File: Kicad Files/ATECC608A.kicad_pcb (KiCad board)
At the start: 2 copper layers, 26.7 x 22.8 mm, 17 parts, among them J1 Conn_01x04, U1 ATECC608A-SSHDA

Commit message: logos review
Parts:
- added G***: LOGO, Aesthetics:SDA, B.Cu at (168.6, 47.0)
- added G***: LOGO, Aesthetics:SCL, B.Cu at (166.2, 47.1)
- added G***: LOGO, Aesthetics:GND, B.Cu at (163.6, 47.1)
- added G***: LOGO, Aesthetics:3v3, B.Cu at (161.0, 47.1)
- J1: moved to B.Cu
- moved REF** 1.41 mm to (155.3, 43.0)
- moved G*** 0.15 mm to (164.8, 34.5)
- turned J1 to 270 degrees

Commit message: logos
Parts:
- moved G*** 0.48 mm to (166.0, 47.1)
- moved G*** 0.45 mm to (168.5, 47.1)
- moved G*** 0.40 mm to (163.4, 47.1)
- moved G*** 0.40 mm to (160.8, 47.1)
- moved G*** 0.14 mm to (163.7, 47.0)
- moved G*** 0.10 mm to (161.0, 47.0)
- moved G*** 0.08 mm to (166.2, 47.0)
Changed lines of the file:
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@@
-(kicad_pcb (version 20171130) (host pcbnew "(5.1.4-0-10_14)")
+(kicad_pcb (version 20171130) (host pcbnew "(5.1.4)-1")
   (general
     (thickness 1.6)
@@
     (35 F.Paste user)
     (36 B.SilkS user)
-    (37 F.SilkS user hide)
+    (37 F.SilkS user)
     (38 B.Mask user)
     (39 F.Mask user)
@@
     (43 Eco2.User user)
     (44 Edge.Cuts user)
-    (45 Margin user)
+    (45 Margin user hide)
     (46 B.CrtYd user)
     (47 F.CrtYd user)
@@
   )
   (module Aesthetics:SCL (layer B.Cu)
-    (at 166.15 47.125 270)
+    (at 166.15 47.05 270)
     (fp_text reference G*** (at 0 0 90) (layer B.SilkS) hide
       (effects (font (size 1.524 1.524) (thickness 0.3)) (justify mirror))
@@
   )
   (module Aesthetics:GND (layer B.Cu)
-    (at 163.575 47.1 270)
+    (at 163.703 47.05 270)
     (fp_text reference G*** (at 0 0 90) (layer B.SilkS) hide
       (effects (font (size 1.524 1.524) (thickness 0.3)) (justify mirror))
@@
   )
   (module Aesthetics:3v3 (layer B.Cu)
-    (at 161 47.15 270)
+    (at 161 47.05 270)
     (fp_text reference G*** (at 0 0 90) (layer B.SilkS) hide
       (effects (font (size 1.524 1.524) (thickness 0.3)) (justify mirror))
@@
   )
   (module GND (layer F.Cu)
-    (at 163.5 47.45 90)
+    (at 163.4238 47.0555 90)
     (fp_text reference G*** (at 0 0 90) (layer F.SilkS) hide
       (effects (font (size 1.524 1.524) (thickness 0.3)))
@@
   )
   (module 3v3 (layer F.Cu)
-    (at 160.9 47.45 90)
+    (at 160.8238 47.0555 90)
     (fp_text reference G*** (at 0 0 90) (layer F.SilkS) hide
       (effects (font (size 1.524 1.524) (thickness 0.3)))
@@
   )
   (module SCL (layer F.Cu)
-    (at 166.35 47.4 90)
+    (at 166.0144 47.0535 90)
     (fp_text reference G*** (at 0 0 90) (layer F.SilkS) hide
       (effects (font (size 1.524 1.524) (thickness 0.3)))
@@
   )
   (module SDA (layer F.Cu)
-    (at 168.6 47.5 90)
+    (at 168.5238 47.0555 90)
     (fp_text reference G*** (at 0 0 90) (layer F.SilkS) hide
       (effects (font (size 1.524 1.524) (thickness 0.3)))
@@
     (connect_pads (clearance 0.508))
     (min_thickness 0.254)
-    (fill (arc_segments 32) (thermal_gap 0.508) (thermal_bridge_width 0.508))
+    (fill yes (arc_segments 32) (thermal_gap 0.508) (thermal_bridge_width 0.508))
     (polygon
       (pts
@@
     (connect_pads (clearance 0.508))
     (min_thickness 0.254)
-    (fill (arc_segments 32) (thermal_gap 0.508) (thermal_bridge_width 0.508))
+    (fill yes (arc_segments 32) (thermal_gap 0.508) (thermal_bridge_width 0.508))
     (polygon
       (pts

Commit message: add logo front
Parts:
- added G***: LOGO, Aesthetics:electronic_cats_logo_4x3, F.Cu at (174.7, 44.4)
- moved REF** 0.93 mm to (154.9, 43.8)

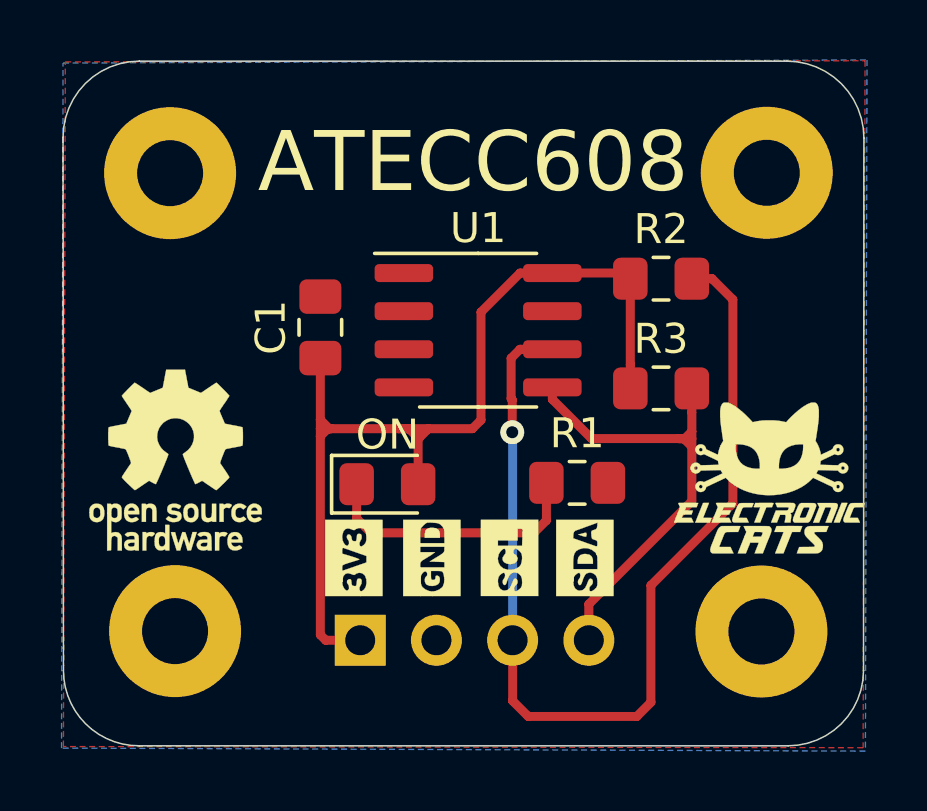
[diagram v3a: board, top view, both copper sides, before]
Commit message: Update to KiCad 6.0
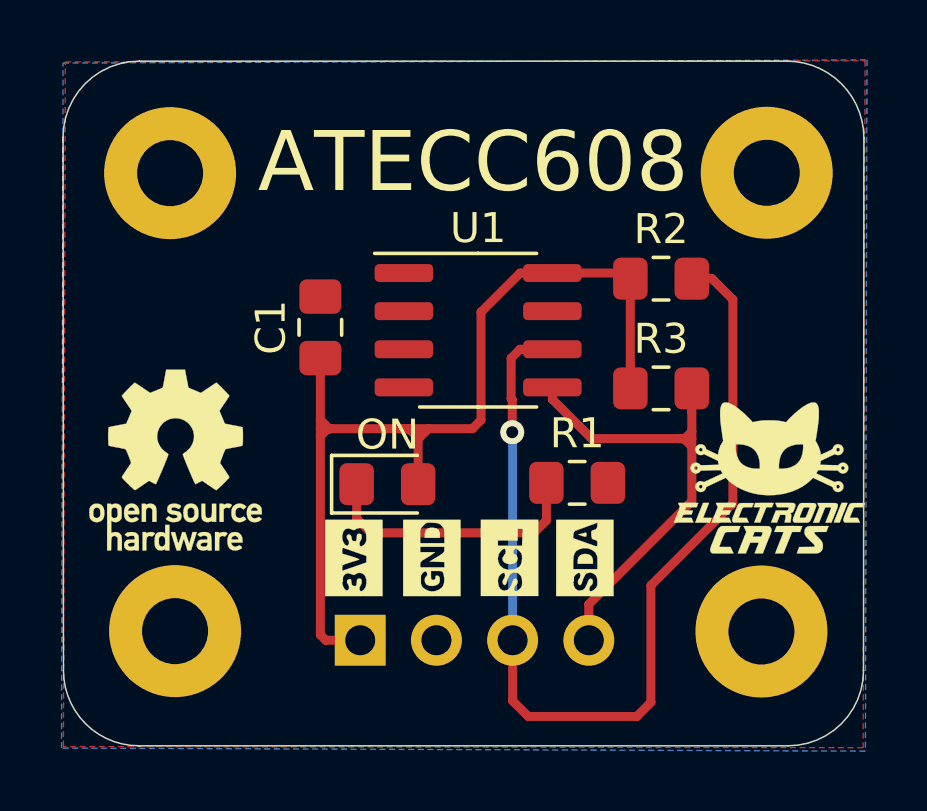
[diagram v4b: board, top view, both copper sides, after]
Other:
- net class Default removed
- net class vcc removed
